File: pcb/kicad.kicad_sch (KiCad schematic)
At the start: 7 parts, among them SW1 SW_Push, SW2 SW_Push, SW3 SW_Push, SW4 SW_Push, U1 XIAO-RP2040-DIP

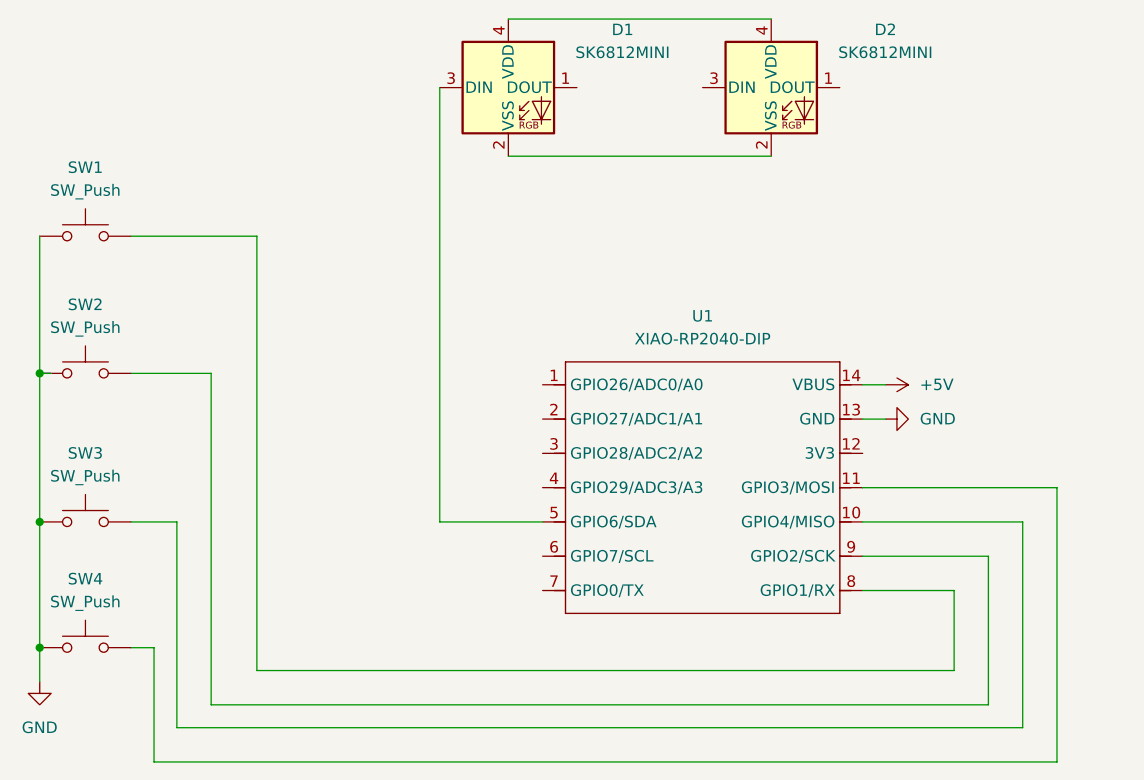
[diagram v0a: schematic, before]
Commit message: update cad and pcb to include lcd display
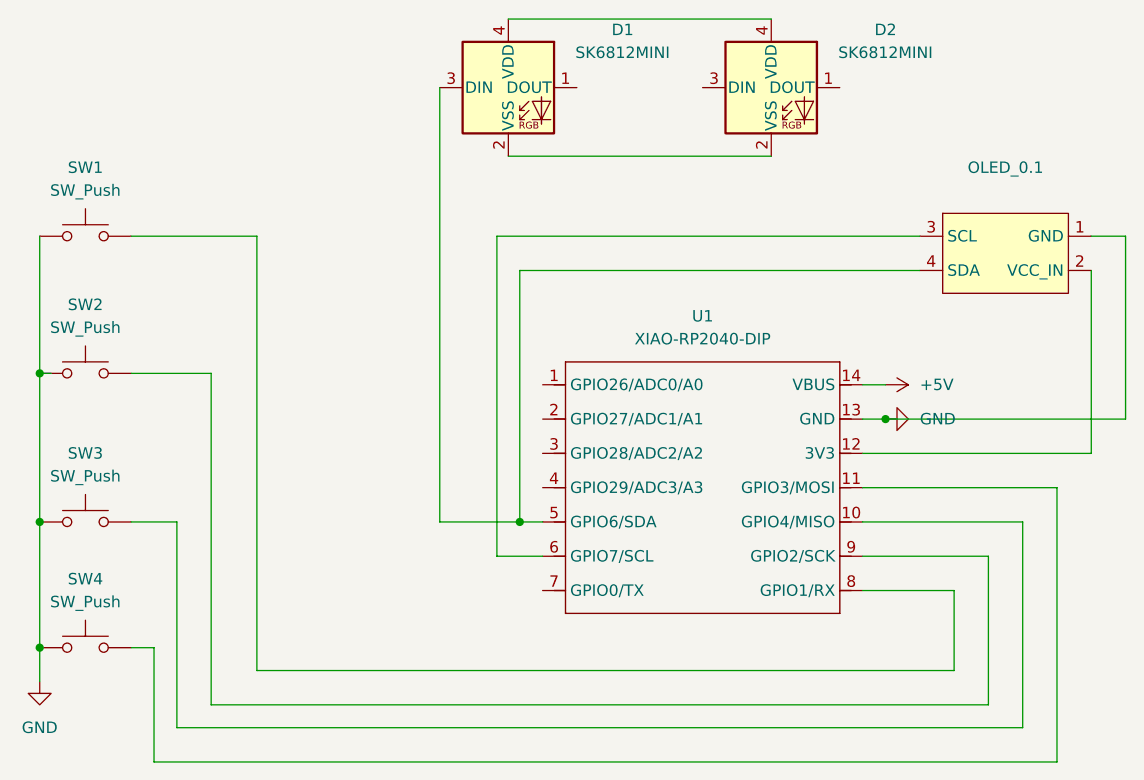
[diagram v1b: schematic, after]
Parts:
- added OLED_0.1: ~, OLED_0.91inch:SSD1306-0.91-OLED-4pin-128x32, symbol OLED_0.91:OLED_0.91
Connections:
- net GND: now also OLED_0.1.1 (GND)
- net at D1.3 (DIN), U1.5 (GPIO6/SDA): now also OLED_0.1.4 (SDA)
- net at U1.12 (3V3): now also OLED_0.1.2 (VCC_IN)
- net at U1.6 (GPIO7/SCL): now also OLED_0.1.3 (SCL)
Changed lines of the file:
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@@
 	(paper "A4")
+	(junction
+		(at 124.46 127)
+		(diameter 0)
+		(color 0 0 0 0)
+	)
+	(junction
+		(at 165.1 115.57)
+		(diameter 0)
+		(color 0 0 0 0)
+	)
 	(junction
 		(at 71.12 110.49)
@@
 	(wire
 		(pts
-			(xy 115.57 127) (xy 127 127)
+			(xy 115.57 127) (xy 124.46 127)
 		)
 		(stroke
@@
 	(wire
 		(pts
+			(xy 124.46 127) (xy 127 127)
+		)
+		(stroke
+			(width 0)
+			(type default)
+		)
+	)
+	(wire
+		(pts
+			(xy 187.96 99.06) (xy 187.96 119.38)
+		)
+		(stroke
+			(width 0)
+			(type default)
+		)
+	)
+	(wire
+		(pts
+			(xy 191.77 115.57) (xy 165.1 115.57)
+		)
+		(stroke
+			(width 0)
+			(type default)
+		)
+	)
+	(wire
+		(pts
 			(xy 180.34 149.86) (xy 180.34 127)
 		)
@@
 	(wire
 		(pts
+			(xy 187.96 95.25) (xy 191.77 95.25)
+		)
+		(stroke
+			(width 0)
+			(type default)
+		)
+	)
+	(wire
+		(pts
+			(xy 121.92 130.81) (xy 127 130.81)
+		)
+		(stroke
+			(width 0)
+			(type default)
+		)
+	)
+	(wire
+		(pts
+			(xy 124.46 99.06) (xy 124.46 127)
+		)
+		(stroke
+			(width 0)
+			(type default)
+		)
+	)
+	(wire
+		(pts
 			(xy 90.17 110.49) (xy 90.17 147.32)
 		)
@@
 	(wire
 		(pts
+			(xy 168.91 95.25) (xy 121.92 95.25)
+		)
+		(stroke
+			(width 0)
+			(type default)
+		)
+	)
+	(wire
+		(pts
 			(xy 81.28 140.97) (xy 83.82 140.97)
 		)
@@
 	(wire
 		(pts
+			(xy 191.77 95.25) (xy 191.77 115.57)
+		)
+		(stroke
+			(width 0)
+			(type default)
+		)
+	)
+	(wire
+		(pts
 			(xy 95.25 143.51) (xy 172.72 143.51)
 		)
@@
 	(wire
 		(pts
+			(xy 187.96 119.38) (xy 162.56 119.38)
+		)
+		(stroke
+			(width 0)
+			(type default)
+		)
+	)
+	(wire
+		(pts
 			(xy 71.12 110.49) (xy 71.12 127)
 		)
@@
 	(wire
 		(pts
+			(xy 121.92 95.25) (xy 121.92 130.81)
+		)
+		(stroke
+			(width 0)
+			(type default)
+		)
+	)
+	(wire
+		(pts
 			(xy 176.53 147.32) (xy 176.53 130.81)
 		)
@@
 		(pts
 			(xy 81.28 127) (xy 86.36 127)
+		)
+		(stroke
+			(width 0)
+			(type default)
+		)
+	)
+	(wire
+		(pts
+			(xy 168.91 99.06) (xy 124.46 99.06)
 		)
 		(stroke
@@
 	)
 	(symbol
+		(lib_id "OLED_0.91:OLED_0.91")
+		(at 171.45 101.6 0)
+		(unit 1)
+		(exclude_from_sim no)
+		(in_bom yes)
+		(on_board yes)
+		(dnp no)
+		(fields_autoplaced yes)
+		(property "Reference" "OLED_0.1"
+			(at 178.435 87.63 0)
+			(effects
+				(font
+					(size 1.27 1.27)
+				)
+			)
+		)
+		(property "Value" "~"
+			(at 178.435 90.17 0)
+			(effects
+				(font
+					(size 1.27 1.27)
+				)
+			)
+		)
+		(property "Footprint" "OLED_0.91inch:SSD1306-0.91-OLED-4pin-128x32"
+			(at 171.45 101.6 0)
+			(effects
+				(font
+					(size 1.27 1.27)
+				)
+				(hide yes)
+			)
+		)
+		(property "Datasheet" ""
+			(at 171.45 101.6 0)
+			(effects
+				(font
+					(size 1.27 1.27)
+				)
+				(hide yes)
+			)
+		)
+		(property "Description" ""
+			(at 171.45 101.6 0)
+			(effects
+				(font
+					(size 1.27 1.27)
+				)
+				(hide yes)
+			)
+		)
+		(pin "3"
+		)
+		(pin "4"
+		)
+		(pin "1"
+		)
+		(pin "2"
+		)
+		(instances
+			(project ""
+				(path "/ab3f720b-55e1-44b6-96f0-cd7675d9a85f"
+					(reference "OLED_0.1")
+					(unit 1)
+				)
+			)
+		)
+	)
+	(symbol
 		(lib_id "LED:SK6812MINI")
 		(at 152.4 78.74 0)
@@
 		(on_board yes)
 		(dnp no)
-		(fields_autoplaced yes)
 		(property "Reference" "D2"
 			(at 165.1 72.3198 0)
